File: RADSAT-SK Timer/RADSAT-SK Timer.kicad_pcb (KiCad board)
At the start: 2 copper layers, 90.2 x 95.9 mm, 102 parts, among them J101 Conn_02x26_Odd_Even, J103 Conn_02x26_Odd_Even, J201 Conn_01x04, J202 USB_B_Micro, J203 Conn_01x02, J204 Conn_01x02, J205 Conn_01x02, J206 Conn_01x02, J207 Conn_01x02, Q101 IRLML2060, Q102 IRLML2060, Q103 IRLML2060, Q104 IRLML2060, Q105 IRLML2060, Q106 IRLML2060, Q107 IRLML2060, Q108 IRLML2060, Q109 IRLML2060, Q201 IRLML2060, Q202 IRLML2060, SW201 SW_Push, SW202 SW_Push, SW203 SW_Push, SW204 SW_Push, SW205 SW_Push, SW206 SW_Push, U101 LM397MF, U102 LM397MF, U103 LM397MF, U104 CD4052B, U202 LTC3440EMSPBF

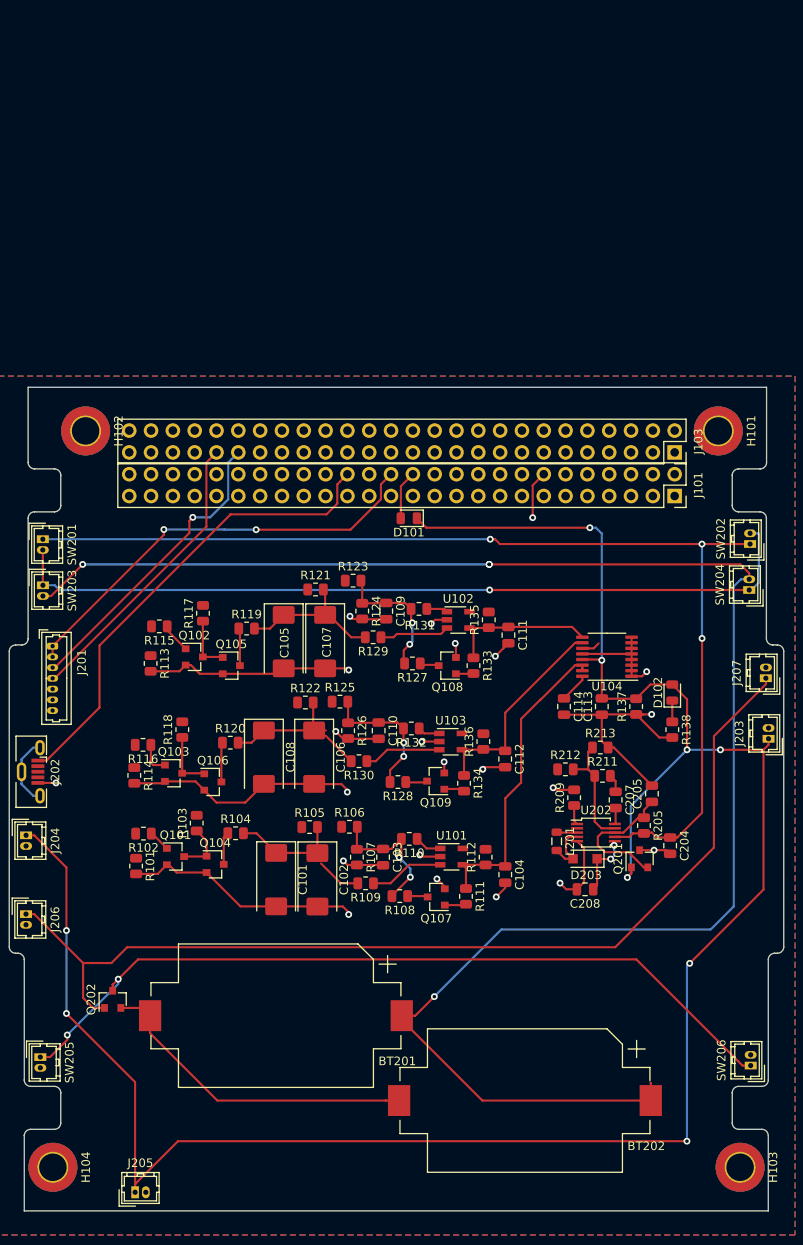
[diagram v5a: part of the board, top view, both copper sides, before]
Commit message: added RBF stuff to PCB
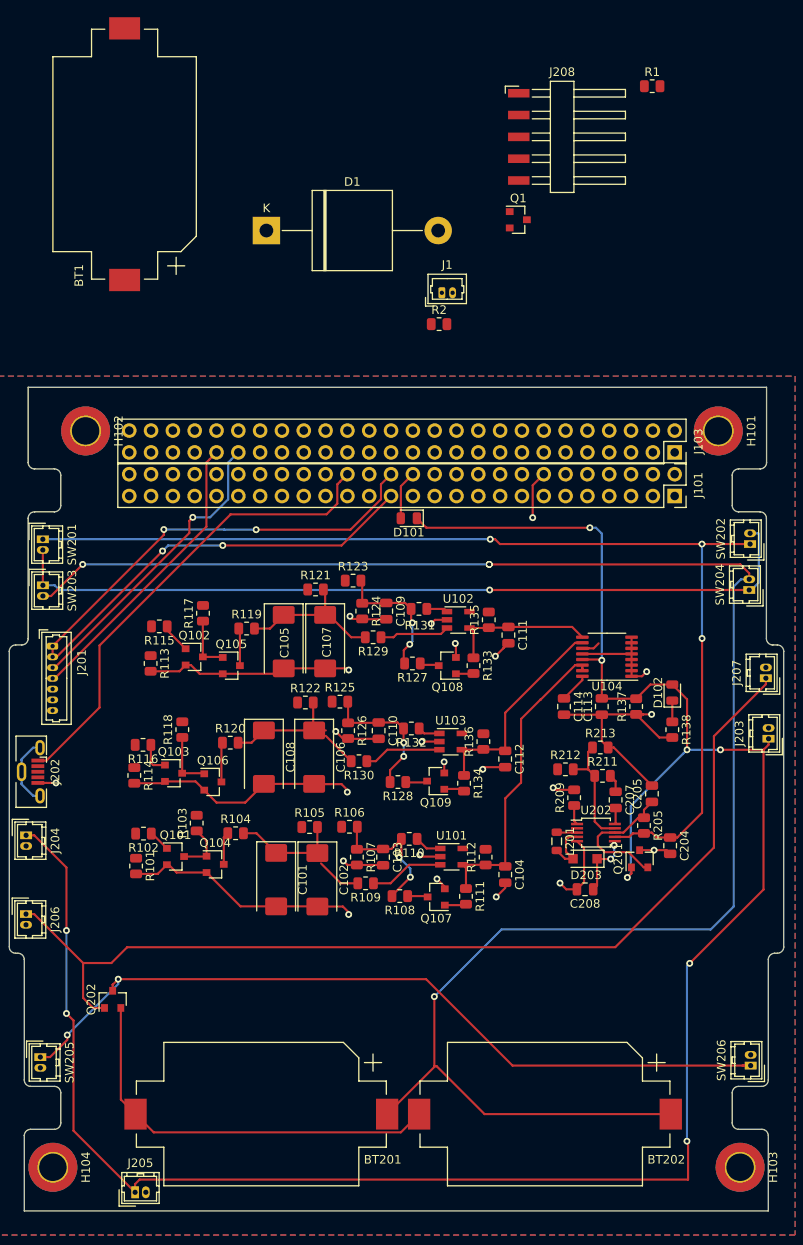
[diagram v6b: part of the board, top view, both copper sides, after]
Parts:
- added BT1: Battery_Cell, Battery:BatteryHolder_Keystone_1060_1x2032, F.Cu at (48.3, 22.9)
- added D1: 5KPxxA, Diode_THT:D_P600_R-6_P20.00mm_Horizontal, F.Cu at (64.8, 31.8)
- added J1: Conn_01x02_Male, Connector_Molex:Molex_PicoBlade_53047-0210_1x02_P1.25mm_Vertical, F.Cu at (85.2, 39.0)
- added J208: Conn_01x05_Male, Connector_Harwin:Harwin_M20-89005xx_1x05_P2.54mm_Horizontal, F.Cu at (99.7, 20.8)
- added Q1: Q_NMOS_DGS, Package_TO_SOT_SMD:SOT-23, F.Cu at (94.1, 30.5)
- added R1: R, Resistor_SMD:R_0805_2012Metric, F.Cu at (109.7, 14.9)
- added R2: R, Resistor_SMD:R_0805_2012Metric, F.Cu at (84.9, 42.6)
- J201: value Conn_01x04 -> Conn_01x07
- moved BT201 11.6 mm to (64.2, 134.6)
- moved BT202 2.82 mm to (97.2, 134.6)
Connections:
- J101 pad 1: (no net) -> Net-(J101-Pad1)
- J101 pad 10: (no net) -> Net-(J101-Pad10)
- J101 pad 11: (no net) -> Net-(J101-Pad11)
- J101 pad 12: (no net) -> Net-(J101-Pad12)
- J101 pad 13: (no net) -> Net-(J101-Pad13)
- J101 pad 15: (no net) -> Net-(J101-Pad15)
- J101 pad 16: (no net) -> Net-(J101-Pad16)
- J101 pad 17: (no net) -> Net-(J101-Pad17)
- J101 pad 18: (no net) -> Net-(J101-Pad18)
- J101 pad 19: (no net) -> Net-(J101-Pad19)
- J101 pad 2: (no net) -> Net-(J101-Pad2)
- J101 pad 20: (no net) -> Net-(J101-Pad20)
- J101 pad 21: (no net) -> Net-(J101-Pad21)
- J101 pad 22: (no net) -> Net-(J101-Pad22)
- J101 pad 23: (no net) -> Net-(J101-Pad23)
- J101 pad 24: (no net) -> Net-(J101-Pad24)
- J101 pad 25: (no net) -> Net-(J101-Pad25)
- J101 pad 27: (no net) -> Net-(J101-Pad27)
- J101 pad 29: (no net) -> Net-(J101-Pad29)
- J101 pad 3: (no net) -> Net-(J101-Pad3)
- J101 pad 30: (no net) -> Net-(J101-Pad30)
- J101 pad 31: (no net) -> Net-(J101-Pad31)
- J101 pad 32: USB_Charge -> Net-(J101-Pad32)
- J101 pad 33: (no net) -> Net-(J101-Pad33)
- J101 pad 34: (no net) -> Net-(J101-Pad34)
- J101 pad 35: (no net) -> Net-(J101-Pad35)
- J101 pad 36: (no net) -> Net-(J101-Pad36)
- J101 pad 37: (no net) -> Net-(J101-Pad37)
- J101 pad 38: (no net) -> Net-(J101-Pad38)
- J101 pad 39: (no net) -> Net-(J101-Pad39)
- J101 pad 4: (no net) -> Net-(J101-Pad4)
- J101 pad 40: (no net) -> Net-(J101-Pad40)
- J101 pad 41: (no net) -> Net-(J101-Pad41)
- J101 pad 42: (no net) -> Net-(J101-Pad42)
- J101 pad 43: (no net) -> Net-(J101-Pad43)
- J101 pad 44: (no net) -> Net-(J101-Pad44)
- J101 pad 45: (no net) -> Net-(J101-Pad45)
- J101 pad 46: (no net) -> Net-(J101-Pad46)
- J101 pad 47: (no net) -> Net-(J101-Pad47)
- J101 pad 48: (no net) -> Net-(J101-Pad48)
- J101 pad 49: (no net) -> Net-(J101-Pad49)
- J101 pad 5: (no net) -> Net-(J101-Pad5)
- J101 pad 50: (no net) -> Net-(J101-Pad50)
- J101 pad 51: (no net) -> Net-(J101-Pad51)
- J101 pad 52: (no net) -> Net-(J101-Pad52)
- J101 pad 6: (no net) -> Net-(J101-Pad6)
- J101 pad 7: (no net) -> Net-(J101-Pad7)
- J101 pad 8: (no net) -> Net-(J101-Pad8)
- J101 pad 9: (no net) -> Net-(J101-Pad9)
- J103 pad 1: (no net) -> Net-(J103-Pad1)
- J103 pad 10: (no net) -> Net-(J103-Pad10)
- J103 pad 11: (no net) -> Net-(J103-Pad11)
- J103 pad 12: (no net) -> Net-(J103-Pad12)
- J103 pad 13: (no net) -> Net-(J103-Pad13)
- J103 pad 14: (no net) -> Net-(J103-Pad14)
- J103 pad 15: (no net) -> Net-(J103-Pad15)
- J103 pad 16: (no net) -> Net-(J103-Pad16)
- J103 pad 17: (no net) -> Net-(J103-Pad17)
- J103 pad 18: (no net) -> Net-(J103-Pad18)
- J103 pad 19: (no net) -> Net-(J103-Pad19)
- J103 pad 2: (no net) -> Net-(J103-Pad2)
- J103 pad 20: (no net) -> Net-(J103-Pad20)
- J103 pad 21: (no net) -> Net-(J103-Pad21)
- J103 pad 22: (no net) -> Net-(J103-Pad22)
- J103 pad 23: (no net) -> Net-(J103-Pad23)
- J103 pad 24: (no net) -> Net-(J103-Pad24)
- J103 pad 25: (no net) -> Net-(J103-Pad25)
- J103 pad 26: (no net) -> Net-(J103-Pad26)
- J103 pad 27: (no net) -> Net-(J103-Pad27)
- J103 pad 28: (no net) -> Net-(J103-Pad28)
- J103 pad 29: (no net) -> Net-(J103-Pad29)
- J103 pad 3: (no net) -> Net-(J103-Pad3)
- J103 pad 30: (no net) -> Net-(J103-Pad30)
- J103 pad 31: (no net) -> Net-(J103-Pad31)
- J103 pad 32: (no net) -> Net-(J103-Pad32)
- J103 pad 33: (no net) -> Net-(J103-Pad33)
- J103 pad 34: (no net) -> Net-(J103-Pad34)
- J103 pad 35: (no net) -> Net-(J103-Pad35)
- J103 pad 36: (no net) -> Net-(J103-Pad36)
- J103 pad 37: (no net) -> Net-(J103-Pad37)
- J103 pad 38: (no net) -> Net-(J103-Pad38)
- J103 pad 39: (no net) -> Net-(J103-Pad39)
- J103 pad 4: (no net) -> Net-(J103-Pad4)
- J103 pad 40: (no net) -> Net-(J103-Pad40)
- J103 pad 42: (no net) -> Net-(J103-Pad42)
- J103 pad 44: (no net) -> Net-(J103-Pad44)
- J103 pad 45: (no net) -> Net-(J103-Pad45)
- J103 pad 46: (no net) -> Net-(J103-Pad46)
- J103 pad 47: (no net) -> Net-(J103-Pad47)
- J103 pad 48: (no net) -> Net-(J103-Pad48)
- J103 pad 49: (no net) -> Net-(J103-Pad49)
- J103 pad 5: (no net) -> Net-(J103-Pad5)
- J103 pad 50: (no net) -> Net-(J103-Pad50)
- J103 pad 51: (no net) -> Net-(J103-Pad51)
- J103 pad 52: (no net) -> Net-(J103-Pad52)
- J103 pad 6: (no net) -> Net-(J103-Pad6)
- J103 pad 7: (no net) -> Net-(J103-Pad7)
- J103 pad 8: (no net) -> Net-(J103-Pad8)
- J103 pad 9: (no net) -> Net-(J103-Pad9)
- J202 pad 2: (no net) -> Net-(J202-Pad2)
- J202 pad 3: (no net) -> Net-(J202-Pad3)
- J202 pad 4: (no net) -> Net-(J202-Pad4)
- U202 pad 2: (no net) -> Net-(U202-Pad2)
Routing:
- net +3V3: track 50.3 -> 97.5 mm, vias 2 -> 4
- net Net-(BT201-Pad2): track 38.1 -> 47.8 mm
- net Net-(BT201-Pad1): track 204.1 -> 209.3 mm
- net BUS_EN: track 254.5 -> 257.3 mm
- net Net-(Q202-Pad3): track 95.2 -> 94.2 mm

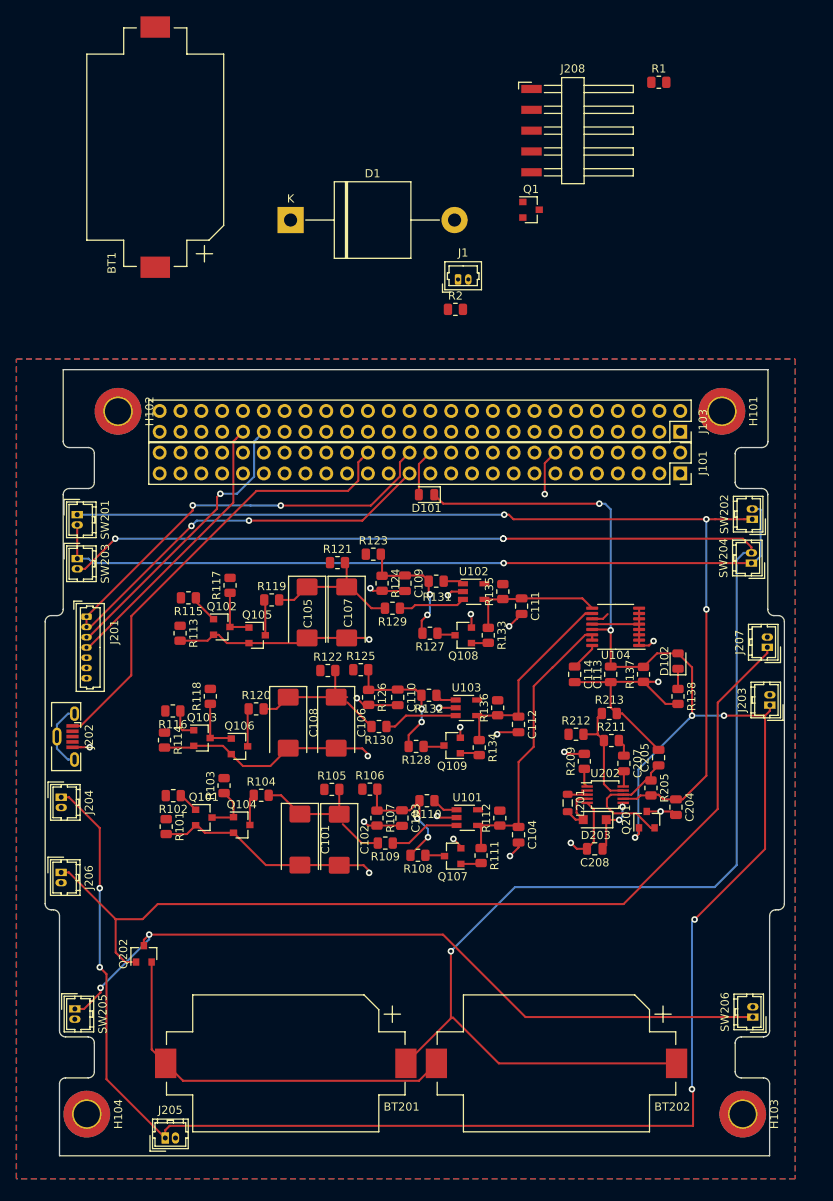
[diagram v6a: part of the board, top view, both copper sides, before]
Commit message: Revert "Retrace (#8)" (#11)
This reverts commit b83679d15abd0ed1c357c8fd6e32726f91c1f504.
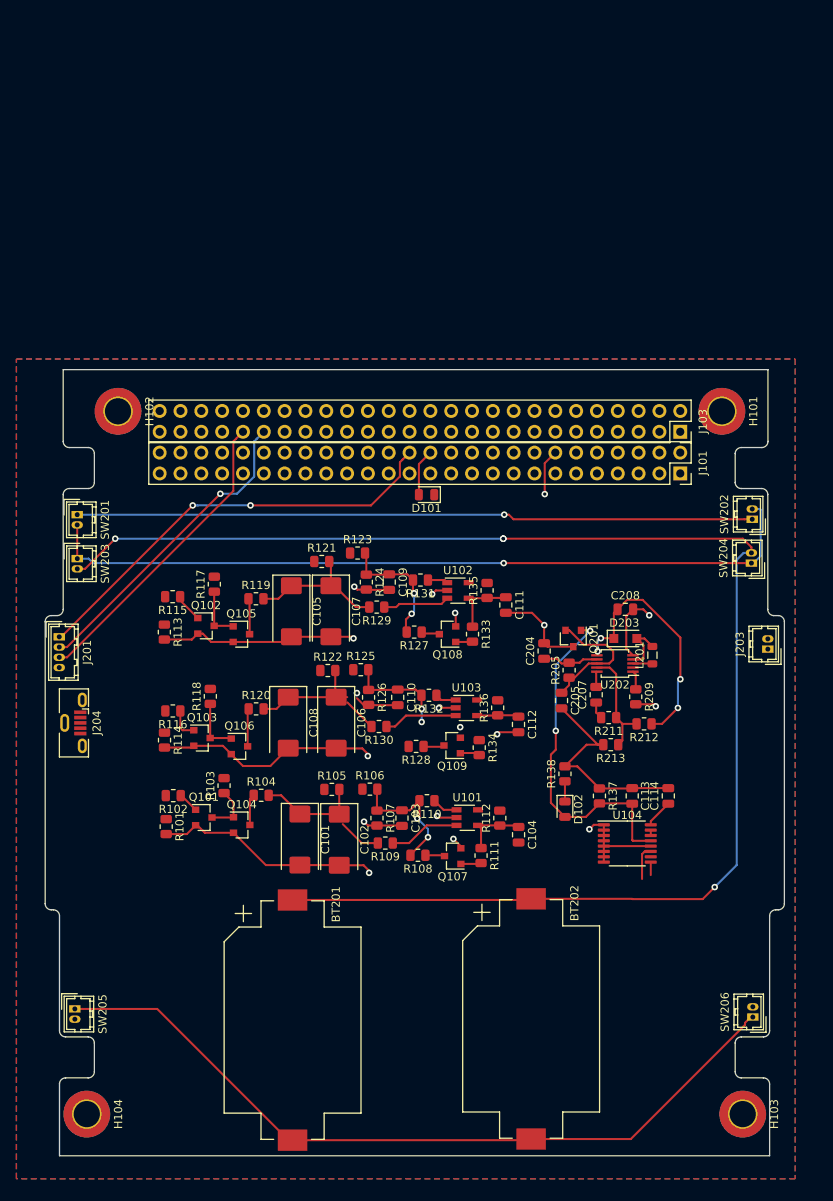
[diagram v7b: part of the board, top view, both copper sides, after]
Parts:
- removed BT1: Battery_Cell, Battery:BatteryHolder_Keystone_1060_1x2032
- removed D1: 5KPxxA, Diode_THT:D_P600_R-6_P20.00mm_Horizontal
- removed J1: Conn_01x02_Male, Connector_Molex:Molex_PicoBlade_53047-0210_1x02_P1.25mm_Vertical
- removed J202: USB_B_Micro, Connector_USB:USB_Micro-B_Molex-105133-0001
- removed J205, J206, J207: Conn_01x02, Connector_Hirose:Hirose_DF13-02P-1.25DSA_1x02_P1.25mm_Vertical
- removed J208: Conn_01x05_Male, Connector_Harwin:Harwin_M20-89005xx_1x05_P2.54mm_Horizontal
- removed Q1: Q_NMOS_DGS, Package_TO_SOT_SMD:SOT-23
- removed Q202: IRLML2060, Package_TO_SOT_SMD:SOT-23
- removed R1, R2: R, Resistor_SMD:R_0805_2012Metric
- J201: value Conn_01x07 -> Conn_01x04; footprint Connector_Molex:Molex_PicoBlade_53047-0710_1x07_P1.25mm_Vertical -> Connector_Hirose:Hirose_DF13-04P-1.25DSA_1x04_P1.25mm_Vertical
- J204: value Conn_01x02 -> USB_B_Micro; footprint Connector_Hirose:Hirose_DF13-02P-1.25DSA_1x02_P1.25mm_Vertical -> Connector_USB:USB_Micro-B_Molex-105133-0001
- moved C208 29.4 mm to (105.6, 79.2), turned to 0 degrees
- moved U104 26.5 mm to (105.8, 107.8), turned to 0 degrees
- moved C204 24.9 mm to (95.7, 84.3), turned to 90 degrees
- moved Q201 23.8 mm to (99.3, 82.8), turned to 270 degrees
- moved D102 22.7 mm to (98.2, 103.6), turned to 270 degrees
- moved D203 22.4 mm to (105.6, 82.8), turned to 0 degrees
- moved L201 20.8 mm to (108.9, 84.8), turned to 90 degrees
- moved C114 18.7 mm to (110.8, 102.0), turned to 90 degrees
- moved R205 17.5 mm to (98.7, 86.7), turned to 90 degrees
- moved R138 16.7 mm to (98.2, 99.3), turned to 90 degrees
- moved U202 16.0 mm to (104.3, 85.8), turned to 180 degrees
- moved R137 15.8 mm to (102.4, 102.0), turned to 270 degrees
- moved C113 15.1 mm to (106.4, 102.0), turned to 90 degrees
- moved C205 13.7 mm to (97.8, 90.4), turned to 270 degrees
- moved R209 10.1 mm to (106.9, 89.9), turned to 270 degrees
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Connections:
- J101 pad 1: Net-(J101-Pad1) -> (no net)
- J101 pad 10: Net-(J101-Pad10) -> (no net)
- J101 pad 11: Net-(J101-Pad11) -> (no net)
- J101 pad 12: Net-(J101-Pad12) -> (no net)
- J101 pad 13: Net-(J101-Pad13) -> (no net)
- J101 pad 15: Net-(J101-Pad15) -> (no net)
- J101 pad 16: Net-(J101-Pad16) -> (no net)
- J101 pad 17: Net-(J101-Pad17) -> (no net)
- J101 pad 18: Net-(J101-Pad18) -> (no net)
- J101 pad 19: Net-(J101-Pad19) -> (no net)
- J101 pad 2: Net-(J101-Pad2) -> (no net)
- J101 pad 20: Net-(J101-Pad20) -> (no net)
- J101 pad 21: Net-(J101-Pad21) -> (no net)
- J101 pad 22: Net-(J101-Pad22) -> (no net)
- J101 pad 23: Net-(J101-Pad23) -> (no net)
- J101 pad 24: Net-(J101-Pad24) -> (no net)
- J101 pad 25: Net-(J101-Pad25) -> (no net)
- J101 pad 27: Net-(J101-Pad27) -> (no net)
- J101 pad 29: Net-(J101-Pad29) -> (no net)
- J101 pad 3: Net-(J101-Pad3) -> (no net)
- J101 pad 30: Net-(J101-Pad30) -> (no net)
- J101 pad 31: Net-(J101-Pad31) -> (no net)
- J101 pad 32: Net-(J101-Pad32) -> (no net)
- J101 pad 33: Net-(J101-Pad33) -> (no net)
- J101 pad 34: Net-(J101-Pad34) -> (no net)
- J101 pad 35: Net-(J101-Pad35) -> (no net)
- J101 pad 36: Net-(J101-Pad36) -> (no net)
- J101 pad 37: Net-(J101-Pad37) -> (no net)
- J101 pad 38: Net-(J101-Pad38) -> (no net)
- J101 pad 39: Net-(J101-Pad39) -> (no net)
- J101 pad 4: Net-(J101-Pad4) -> (no net)
- J101 pad 40: Net-(J101-Pad40) -> (no net)
- J101 pad 41: Net-(J101-Pad41) -> (no net)
- J101 pad 42: Net-(J101-Pad42) -> (no net)
- J101 pad 43: Net-(J101-Pad43) -> (no net)
- J101 pad 44: Net-(J101-Pad44) -> (no net)
- J101 pad 45: Net-(J101-Pad45) -> (no net)
- J101 pad 46: Net-(J101-Pad46) -> (no net)
- J101 pad 47: Net-(J101-Pad47) -> (no net)
- J101 pad 48: Net-(J101-Pad48) -> (no net)
- J101 pad 49: Net-(J101-Pad49) -> (no net)
- J101 pad 5: Net-(J101-Pad5) -> (no net)
- J101 pad 50: Net-(J101-Pad50) -> (no net)
- J101 pad 51: Net-(J101-Pad51) -> (no net)
- J101 pad 52: Net-(J101-Pad52) -> (no net)
- J101 pad 6: Net-(J101-Pad6) -> (no net)
- J101 pad 7: Net-(J101-Pad7) -> (no net)
- J101 pad 8: Net-(J101-Pad8) -> (no net)
- J101 pad 9: Net-(J101-Pad9) -> (no net)
- J103 pad 1: Net-(J103-Pad1) -> (no net)
- J103 pad 10: Net-(J103-Pad10) -> (no net)
- J103 pad 11: Net-(J103-Pad11) -> (no net)
- J103 pad 12: Net-(J103-Pad12) -> (no net)
- J103 pad 13: Net-(J103-Pad13) -> (no net)
- J103 pad 14: Net-(J103-Pad14) -> (no net)
- J103 pad 15: Net-(J103-Pad15) -> (no net)
- J103 pad 16: Net-(J103-Pad16) -> (no net)
- J103 pad 17: Net-(J103-Pad17) -> (no net)
- J103 pad 18: Net-(J103-Pad18) -> (no net)
- J103 pad 19: Net-(J103-Pad19) -> (no net)
- J103 pad 2: Net-(J103-Pad2) -> (no net)
- J103 pad 20: Net-(J103-Pad20) -> (no net)
- J103 pad 21: Net-(J103-Pad21) -> (no net)
- J103 pad 22: Net-(J103-Pad22) -> (no net)
- J103 pad 23: Net-(J103-Pad23) -> (no net)
- J103 pad 24: Net-(J103-Pad24) -> (no net)
- J103 pad 25: Net-(J103-Pad25) -> (no net)
- J103 pad 26: Net-(J103-Pad26) -> (no net)
- J103 pad 27: Net-(J103-Pad27) -> (no net)
- J103 pad 28: Net-(J103-Pad28) -> (no net)
- J103 pad 29: Net-(J103-Pad29) -> (no net)
- J103 pad 3: Net-(J103-Pad3) -> (no net)
- J103 pad 30: Net-(J103-Pad30) -> (no net)
- J103 pad 31: Net-(J103-Pad31) -> (no net)
- J103 pad 32: Net-(J103-Pad32) -> (no net)
- J103 pad 33: Net-(J103-Pad33) -> (no net)
- J103 pad 34: Net-(J103-Pad34) -> (no net)
- J103 pad 35: Net-(J103-Pad35) -> (no net)
- J103 pad 36: Net-(J103-Pad36) -> (no net)
- J103 pad 37: Net-(J103-Pad37) -> (no net)
- J103 pad 38: Net-(J103-Pad38) -> (no net)
- J103 pad 39: Net-(J103-Pad39) -> (no net)
- J103 pad 4: Net-(J103-Pad4) -> (no net)
- J103 pad 40: Net-(J103-Pad40) -> (no net)
- J103 pad 42: Net-(J103-Pad42) -> (no net)
- J103 pad 44: Net-(J103-Pad44) -> (no net)
- J103 pad 45: Net-(J103-Pad45) -> (no net)
- J103 pad 46: Net-(J103-Pad46) -> (no net)
- J103 pad 47: Net-(J103-Pad47) -> (no net)
- J103 pad 48: Net-(J103-Pad48) -> (no net)
- J103 pad 49: Net-(J103-Pad49) -> (no net)
- J103 pad 5: Net-(J103-Pad5) -> (no net)
- J103 pad 50: Net-(J103-Pad50) -> (no net)
- J103 pad 51: Net-(J103-Pad51) -> (no net)
- J103 pad 52: Net-(J103-Pad52) -> (no net)
- J103 pad 6: Net-(J103-Pad6) -> (no net)
- J103 pad 7: Net-(J103-Pad7) -> (no net)
- J103 pad 8: Net-(J103-Pad8) -> (no net)
- J103 pad 9: Net-(J103-Pad9) -> (no net)
- J201 pad 2: +3V3 -> I2C_DATA
- J201 pad 3: I2C_DATA -> I2C_CLK
- J201 pad 4: I2C_CLK -> GND
- J204 pad 1: BUS_EN -> (no net)
- J204 pad 2: GND -> (no net)
- SW205 pad 1: Net-(Q202-Pad3) -> Net-(BT201-Pad2)
- SW206 pad 1: Net-(Q202-Pad3) -> Net-(BT201-Pad2)
- U202 pad 2: Net-(U202-Pad2) -> (no net)
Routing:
- net BUS_EN: track 257.3 -> 42.2 mm, vias 9 -> 2
- net /RADSAT-SK Timer 2/RBF: track 117.3 -> 0.00 mm
- net Net-(Q202-Pad3): track 94.2 -> 0.00 mm, vias 2 -> 0
- net USB_Charge: track 55.4 -> 0.00 mm
- net Net-(BT201-Pad2): track 47.8 -> 95.7 mm
- net +3V3: track 97.5 -> 53.1 mm, vias 4 -> 2
- net Net-(C204-Pad1): track 125.6 -> 89.5 mm, vias 3 -> 1
- net Net-(BT201-Pad1): track 209.3 -> 180.3 mm
- net Timer_A_out: track 36.6 -> 8.59 mm
- net +BATT: track 14.0 -> 38.2 mm, vias 2 -> 4
- net Timer_C_out: track 25.1 -> 5.18 mm
- net Net-(J202-Pad6): track 8.32 -> 0.00 mm
- net Timer_B_out: track 17.4 -> 9.83 mm
- net Net-(C110-Pad1): track 15.9 -> 12.3 mm
- net I2C_CLK: track 34.4 -> 37.3 mm
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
